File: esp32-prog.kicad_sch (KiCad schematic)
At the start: 64 parts, among them J2 Conn-02x05_PZ254-2-05-Z-8.5, J2 TYPE-C-31-M-12, Q1 AO3401A, Q2 AO3401A, Q3 AO3400A, Q4 AO3400A, SW1 SW_DIP_x02_50mil_1.27mm_TP-02, U2 CP2102-GMR, U3 LD39200DPUR, U3 TI_SN74LVC1G125DRYR, U4 TI_SN74LVC1G125DRYR, U5 TI_SN74LVC1G125DRYR, U6 TI_SN74LVC1G125DRYR

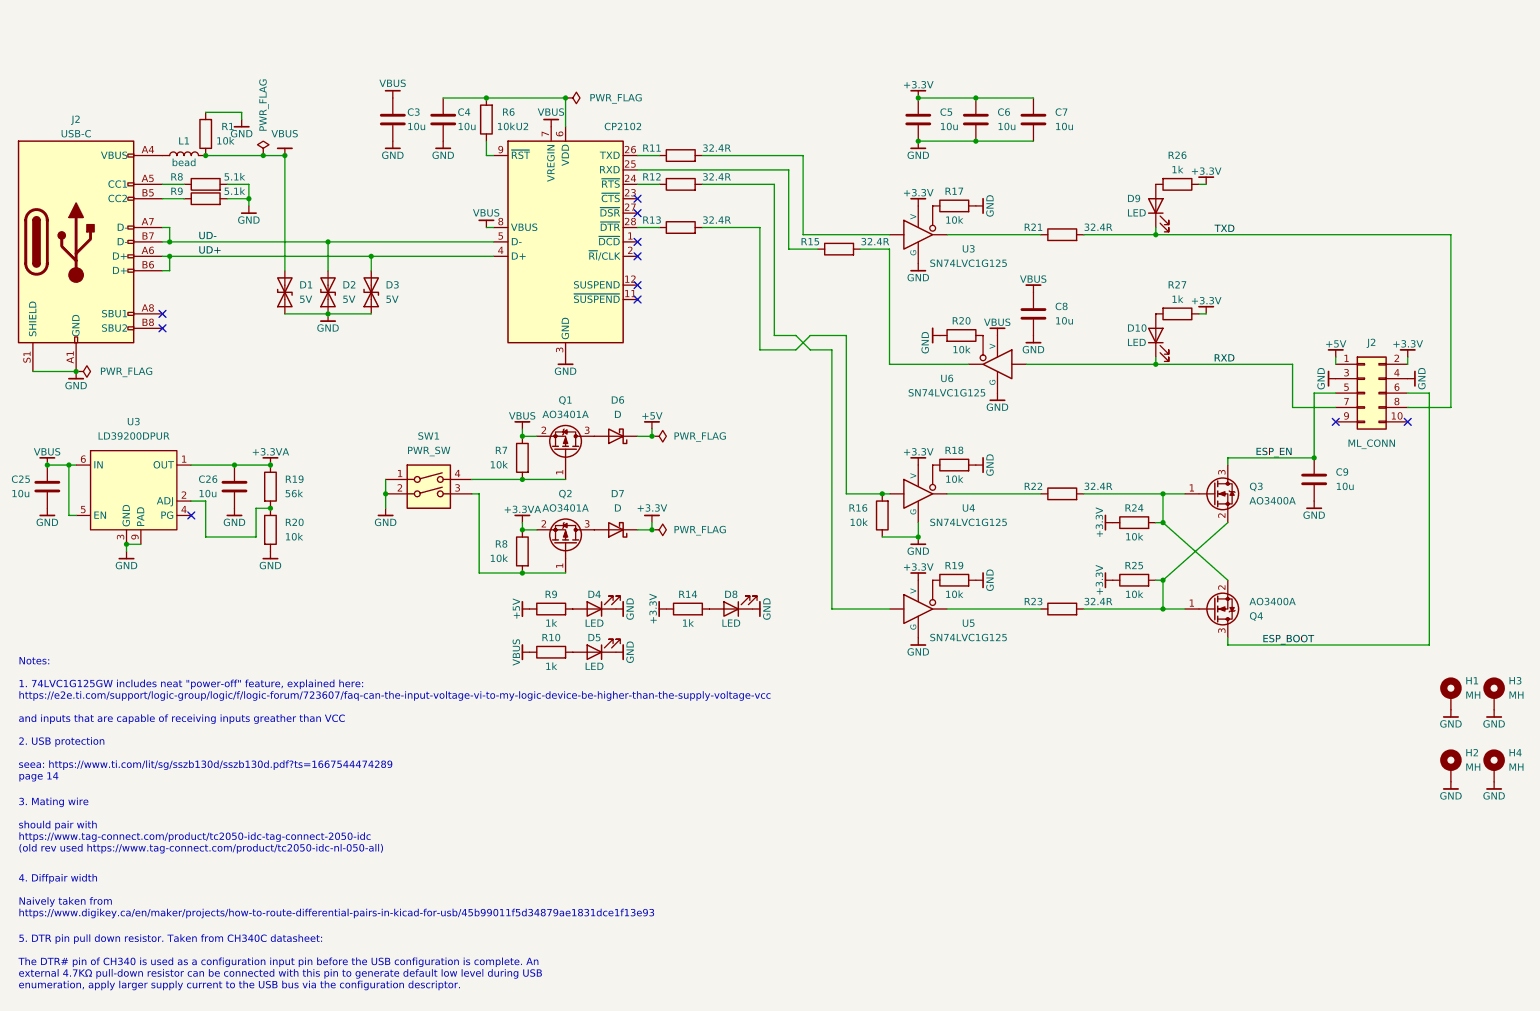
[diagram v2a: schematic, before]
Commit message: address the incorect pinout of the LD39200DPUR
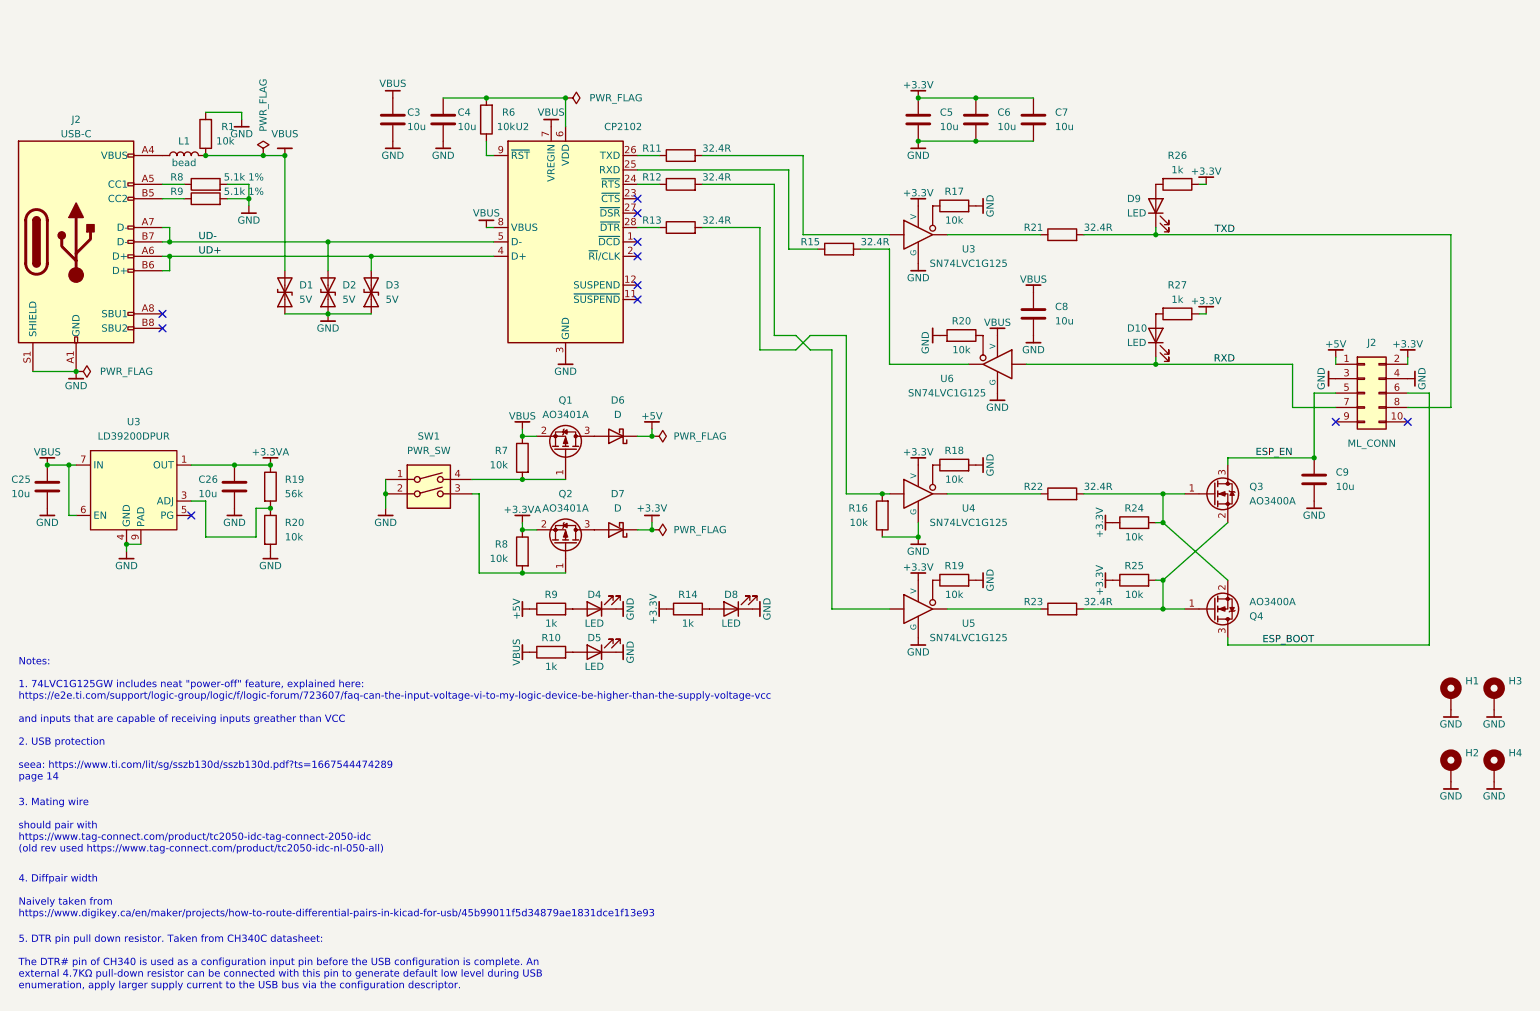
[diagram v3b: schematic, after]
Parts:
- H1, H2, H3, H4: value MH -> MountingHole_Pad; footprint MountingHole:MountingHole_3.2mm_M3_ISO7380_Pad -> (none)
- Q3, Q4: LNK1 (none) -> https://jlcpcb.com/partdetail/Alpha_OmegaSemicon-AO3400A/C2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; SNB1 Basic part -> Basic Part
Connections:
- net +3.3VA: now also U3.2 (OUT)
- net GND: now also U3.4 (GND); no longer U3.3 (GND)
- net VBUS: now also U3.7 (IN), U3.8 (IN); no longer U3.5 (EN)
- net at R19.2, R20.1: now also U3.3 (ADJ); no longer U3.2 (ADJ)
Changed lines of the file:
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@@
   (title_block
     (title "ESP32 External Programmer")
-    (date "20230725")
-    (rev "rev2")
+    (date "20240122")
+    (rev "rev3")
     (company "MAXLAB.IO INC.")
   )
@@
     )
     (property "Tolerance" "1%" (at 58.42 50.8 90)
-      (effects (font (size 1.27 1.27)) hide)
+      (effects (font (size 1.27 1.27)))
     )
     (property "MFR" "UNI-ROYAL" (at 19.05 52.07 0)
@@
     )
   )
-  (symbol (lib_name "1k_0402_0402WGF1001TCE_1") (lib_id "00-kiml-resistors-smd:1k_0402_0402WGF1001TCE") (at 220.98 74.93 270) (unit 1)
+  (symbol (lib_id "00-kiml-resistors-smd:1k_0402_0402WGF1001TCE") (at 220.98 74.93 270) (unit 1)
     (in_bom yes) (on_board yes) (dnp no)
     (property "Reference" "R27" (at 220.98 69.85 90)
@@
     )
   )
-  (symbol (lib_name "10k_0402_0402WGF1002TCE_4") (lib_id "00-kiml-resistors-smd:10k_0402_0402WGF1002TCE") (at 105.41 100.33 0) (mirror y) (unit 1)
+  (symbol (lib_id "00-kiml-resistors-smd:10k_0402_0402WGF1002TCE") (at 105.41 100.33 0) (mirror y) (unit 1)
     (in_bom yes) (on_board yes) (dnp no) (fields_autoplaced)
     (property "Reference" "R7" (at 102.87 99.06 0)
@@
     )
   )
-  (symbol (lib_name "10k_0402_0402WGF1002TCE_3") (lib_id "00-kiml-resistors-smd:10k_0402_0402WGF1002TCE") (at 181.61 55.88 90) (unit 1)
+  (symbol (lib_id "00-kiml-resistors-smd:10k_0402_0402WGF1002TCE") (at 181.61 55.88 90) (unit 1)
     (in_bom yes) (on_board yes) (dnp no)
     (property "Reference" "R17" (at 181.61 53.34 90)
@@
     )
   )
-  (symbol (lib_name "10k_0402_0402WGF1002TCE_7") (lib_id "00-kiml-resistors-smd:10k_0402_0402WGF1002TCE") (at 213.36 121.92 90) (unit 1)
+  (symbol (lib_id "00-kiml-resistors-smd:10k_0402_0402WGF1002TCE") (at 213.36 121.92 90) (unit 1)
     (in_bom yes) (on_board yes) (dnp no)
     (property "Reference" "R25" (at 213.36 119.38 90)
@@
     (pin "6")
     (pin "9")
+    (pin "7")
+    (pin "8")
     (instances
       (project "eie-mainpcb-rev3"
@@
     )
   )
-  (symbol (lib_name "10k_0402_0402WGF1002TCE_3") (lib_id "00-kiml-resistors-smd:10k_0402_0402WGF1002TCE") (at 49.53 43.18 180) (unit 1)
+  (symbol (lib_id "00-kiml-resistors-smd:10k_0402_0402WGF1002TCE") (at 49.53 43.18 180) (unit 1)
     (in_bom yes) (on_board yes) (dnp no)
     (property "Reference" "R1" (at 54.61 41.91 0)
@@
     )
   )
-  (symbol (lib_name "1k_0402_0402WGF1001TCE_1") (lib_id "00-kiml-resistors-smd:1k_0402_0402WGF1001TCE") (at 110.49 127 90) (unit 1)
+  (symbol (lib_id "00-kiml-resistors-smd:1k_0402_0402WGF1001TCE") (at 110.49 127 90) (unit 1)
     (in_bom yes) (on_board yes) (dnp no)
     (property "Reference" "R9" (at 110.49 124.46 90)
@@
       (effects (font (size 1.27 1.27)) (justify left))
     )
-    (property "Value" "MH" (at 271.78 154.9399 0)
-      (effects (font (size 1.27 1.27)) (justify left))
+    (property "Value" "MountingHole_Pad" (at 271.78 154.9399 0)
+      (effects (font (size 1.27 1.27)) (justify left) hide)
     )
-    (property "Footprint" "MountingHole:MountingHole_3.2mm_M3_ISO7380_Pad" (at 269.24 154.94 0)
+    (property "Footprint" "" (at 269.24 154.94 0)
       (effects (font (size 1.27 1.27)) hide)
     )
@@
       (effects (font (size 1.27 1.27)) hide)
     )
-    (property "Datasheet" "https://datasheet.lcsc.com/lcsc/1809140216_Jiangsu-Changjing-Electronics-Technology-Co---Ltd--B5819W-SL_C8598.pdf" (at 127 92.71 0)
+    (property "Datasheet" "https://datasheet.lcsc.com/lcsc/2304140030_BORN-SS34_C266553.pdf" (at 127 92.71 0)
       (effects (font (size 1.27 1.27)) hide)
     )
@@
     )
   )
-  (symbol (lib_name "10k_0402_0402WGF1002TCE_4") (lib_id "00-kiml-resistors-smd:10k_0402_0402WGF1002TCE") (at 182.88 78.74 270) (mirror x) (unit 1)
+  (symbol (lib_id "00-kiml-resistors-smd:10k_0402_0402WGF1002TCE") (at 182.88 78.74 270) (mirror x) (unit 1)
     (in_bom yes) (on_board yes) (dnp no)
     (property "Reference" "R20" (at 182.88 76.2 90)
@@
       (effects (font (size 1.27 1.27)) (justify left))
     )
-    (property "Value" "MH" (at 271.78 142.2399 0)
-      (effects (font (size 1.27 1.27)) (justify left))
+    (property "Value" "MountingHole_Pad" (at 271.78 142.2399 0)
+      (effects (font (size 1.27 1.27)) (justify left) hide)
     )
-    (property "Footprint" "MountingHole:MountingHole_3.2mm_M3_ISO7380_Pad" (at 269.24 142.24 0)
+    (property "Footprint" "" (at 269.24 142.24 0)
       (effects (font (size 1.27 1.27)) hide)
     )
@@
     )
   )
-  (symbol (lib_name "10k_0402_0402WGF1002TCE_3") (lib_id "00-kiml-resistors-smd:10k_0402_0402WGF1002TCE") (at 99.06 40.64 180) (unit 1)
+  (symbol (lib_id "00-kiml-resistors-smd:10k_0402_0402WGF1002TCE") (at 99.06 40.64 180) (unit 1)
     (in_bom yes) (on_board yes) (dnp no)
     (property "Reference" "R6" (at 104.14 39.37 0)
@@
       (effects (font (size 1.27 1.27)) hide)
     )
-    (property "SNB1" "Basic part" (at 228.6 97.79 0)
+    (property "SNB1" "Basic Part" (at 228.6 97.79 0)
+      (effects (font (size 1.27 1.27)) hide)
+    )
+    (property "LNK1" "https://jlcpcb.com/partdetail/Alpha_OmegaSemicon-AO3400A/C20917" (at 228.6 105.41 0)
       (effects (font (size 1.27 1.27)) hide)
     )
@@
       (effects (font (size 1.27 1.27)) hide)
     )
-    (property "SNB1" "Basic part" (at 228.6 135.89 0)
+    (property "SNB1" "Basic Part" (at 228.6 135.89 0)
+      (effects (font (size 1.27 1.27)) hide)
+    )
+    (property "LNK1" "https://jlcpcb.com/partdetail/Alpha_OmegaSemicon-AO3400A/C20917" (at 228.6 128.27 0)
       (effects (font (size 1.27 1.27)) hide)
     )
@@
     )
   )
-  (symbol (lib_name "10k_0402_0402WGF1002TCE_2") (lib_id "00-kiml-resistors-smd:10k_0402_0402WGF1002TCE") (at 213.36 111.76 90) (unit 1)
+  (symbol (lib_id "00-kiml-resistors-smd:10k_0402_0402WGF1002TCE") (at 213.36 111.76 90) (unit 1)
     (in_bom yes) (on_board yes) (dnp no)
     (property "Reference" "R24" (at 213.36 109.22 90)
@@
     )
     (property "Tolerance" "1%" (at 58.42 53.34 90)
-      (effects (font (size 1.27 1.27)) hide)
+      (effects (font (size 1.27 1.27)))
     )
     (property "MFR" "UNI-ROYAL" (at 19.05 54.61 0)
@@
     )
   )
-  (symbol (lib_name "1k_0402_0402WGF1001TCE_1") (lib_id "00-kiml-resistors-smd:1k_0402_0402WGF1001TCE") (at 220.98 52.07 270) (unit 1)
+  (symbol (lib_id "00-kiml-resistors-smd:1k_0402_0402WGF1001TCE") (at 220.98 52.07 270) (unit 1)
     (in_bom yes) (on_board yes) (dnp no)
     (property "Reference" "R26" (at 220.98 46.99 90)
@@
       (effects (font (size 1.27 1.27)) hide)
     )
-    (property "Datasheet" "https://datasheet.lcsc.com/lcsc/1809140216_Jiangsu-Changjing-Electronics-Technology-Co---Ltd--B5819W-SL_C8598.pdf" (at 127 76.2 0)
+    (property "Datasheet" "https://datasheet.lcsc.com/lcsc/2304140030_BORN-SS34_C266553.pdf" (at 127 76.2 0)
       (effects (font (size 1.27 1.27)) hide)
     )
@@
     )
   )
-  (symbol (lib_name "10k_0402_0402WGF1002TCE_4") (lib_id "00-kiml-resistors-smd:10k_0402_0402WGF1002TCE") (at 105.41 116.84 0) (mirror y) (unit 1)
+  (symbol (lib_id "00-kiml-resistors-smd:10k_0402_0402WGF1002TCE") (at 105.41 116.84 0) (mirror y) (unit 1)
     (in_bom yes) (on_board yes) (dnp no) (fields_autoplaced)
     (property "Reference" "R8" (at 102.87 115.57 0)
@@
       (effects (font (size 1.27 1.27)) (justify left))
     )
-    (property "Value" "MH" (at 279.4 154.9399 0)
-      (effects (font (size 1.27 1.27)) (justify left))
+    (property "Value" "MountingHole_Pad" (at 279.4 154.9399 0)
+      (effects (font (size 1.27 1.27)) (justify left) hide)
     )
-    (property "Footprint" "MountingHole:MountingHole_3.2mm_M3_ISO7380_Pad" (at 276.86 154.94 0)
+    (property "Footprint" "" (at 276.86 154.94 0)
       (effects (font (size 1.27 1.27)) hide)
     )
@@
     )
   )
-  (symbol (lib_name "10k_0402_0402WGF1002TCE_6") (lib_id "00-kiml-resistors-smd:10k_0402_0402WGF1002TCE") (at 181.61 101.6 90) (unit 1)
+  (symbol (lib_id "00-kiml-resistors-smd:10k_0402_0402WGF1002TCE") (at 181.61 101.6 90) (unit 1)
     (in_bom yes) (on_board yes) (dnp no)
     (property "Reference" "R18" (at 181.61 99.06 90)
@@
     )
   )
-  (symbol (lib_name "10k_0402_0402WGF1002TCE_1") (lib_id "00-kiml-resistors-smd:10k_0402_0402WGF1002TCE") (at 181.61 121.92 90) (unit 1)
+  (symbol (lib_id "00-kiml-resistors-smd:10k_0402_0402WGF1002TCE") (at 181.61 121.92 90) (unit 1)
     (in_bom yes) (on_board yes) (dnp no)
     (property "Reference" "R19" (at 181.61 119.38 90)
@@
     )
   )
-  (symbol (lib_name "1k_0402_0402WGF1001TCE_2") (lib_id "00-kiml-resistors-smd:1k_0402_0402WGF1001TCE") (at 110.49 134.62 90) (unit 1)
+  (symbol (lib_id "00-kiml-resistors-smd:1k_0402_0402WGF1001TCE") (at 110.49 134.62 90) (unit 1)
     (in_bom yes) (on_board yes) (dnp no)
     (property "Reference" "R10" (at 110.49 132.08 90)
@@
     )
   )
-  (symbol (lib_name "10k_0402_0402WGF1002TCE_5") (lib_id "00-kiml-resistors-smd:10k_0402_0402WGF1002TCE") (at 168.91 110.49 180) (unit 1)
+  (symbol (lib_id "00-kiml-resistors-smd:10k_0402_0402WGF1002TCE") (at 168.91 110.49 180) (unit 1)
     (in_bom yes) (on_board yes) (dnp no) (fields_autoplaced)
     (property "Reference" "R16" (at 166.37 109.22 0)
@@
       (effects (font (size 1.27 1.27)) (justify left))
     )
-    (property "Value" "MH" (at 279.4 142.2399 0)
-      (effects (font (size 1.27 1.27)) (justify left))
+    (property "Value" "MountingHole_Pad" (at 279.4 142.2399 0)
+      (effects (font (size 1.27 1.27)) (justify left) hide)
     )
-    (property "Footprint" "MountingHole:MountingHole_3.2mm_M3_ISO7380_Pad" (at 276.86 142.24 0)
+    (property "Footprint" "" (at 276.86 142.24 0)
       (effects (font (size 1.27 1.27)) hide)
     )
